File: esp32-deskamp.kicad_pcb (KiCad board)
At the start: 2 copper layers, 35 parts, among them J1 INPUT 00, J10 ADDITIONAL GPIO, J2 INPUT 01, J3 MUTE, J4 SLEEP, J5 PRE OUT, J6 LFE OUT, J7 INPUT SELECT, J8 MOTOR, J9 12V IN, K1 INPUT 00, K2 INPUT 01, K3 AMP MUTE, K4 AMP SLEEP, Q1 2N3904, Q2 2N3904, Q3 2N3904, Q4 2N3904, U1 ESP32 D1 MINI, U2 TSR 1-2433, U3 L9110

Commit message: Break time
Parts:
- moved J10 130.6 mm to (180.0, 84.5), turned to 90 degrees
- moved Q4 113.3 mm to (180.0, 132.5), turned to 90 degrees
- moved Q3 113.0 mm to (180.0, 120.5), turned to 90 degrees
- moved R4 108.4 mm to (180.0, 136.6), turned to -90 degrees
- moved R3 106.9 mm to (180.0, 124.8), turned to 90 degrees
- moved R2 106.2 mm to (180.0, 113.5), turned to -90 degrees
- moved U1 98.2 mm to (157.3, 92.2), turned to 0 degrees
- moved J7 85.5 mm to (192.2, 77.0), turned to 180 degrees
- moved K4 81.6 mm to (188.9, 137.5), turned to 90 degrees
- moved D4 81.2 mm to (184.6, 137.5), turned to 90 degrees
- moved J9 80.1 mm to (135.0, 107.3), turned to 90 degrees
- moved U2 78.0 mm to (136.4, 96.2)
- moved J4 65.8 mm to (134.2, 137.3), turned to 90 degrees
- moved K3 65.1 mm to (189.0, 125.5), turned to 90 degrees
- moved D3 64.4 mm to (184.7, 125.5), turned to 90 degrees
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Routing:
- net +12V: track 8.72 -> 58.4 mm
- net Net-(J2-Pin_1): track 0.00 -> 48.4 mm
- net Net-(J1-Pin_1): track 0.00 -> 31.2 mm
- net Net-(J1-Pin_2): track 0.00 -> 30.7 mm
- net Net-(J2-Pin_2): track 22.2 -> 44.6 mm
- net PRE_LEFT: track 0.00 -> 12.5 mm
- net PRE_RIGHT: track 0.00 -> 12.5 mm
- net Select2: track 0.00 -> 10.2 mm
- net Net-(D3-A): track 0.00 -> 9.46 mm
- net Net-(D4-A): track 0.00 -> 9.13 mm
- net Net-(J6-Pin_2): track 28.7 -> 19.8 mm
- net Select1: track 0.00 -> 8.18 mm
- net Net-(Q2-B): track 0.00 -> 5.96 mm
- net Net-(Q1-B): track 0.00 -> 5.96 mm
- net Select0: track 0.00 -> 5.50 mm
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
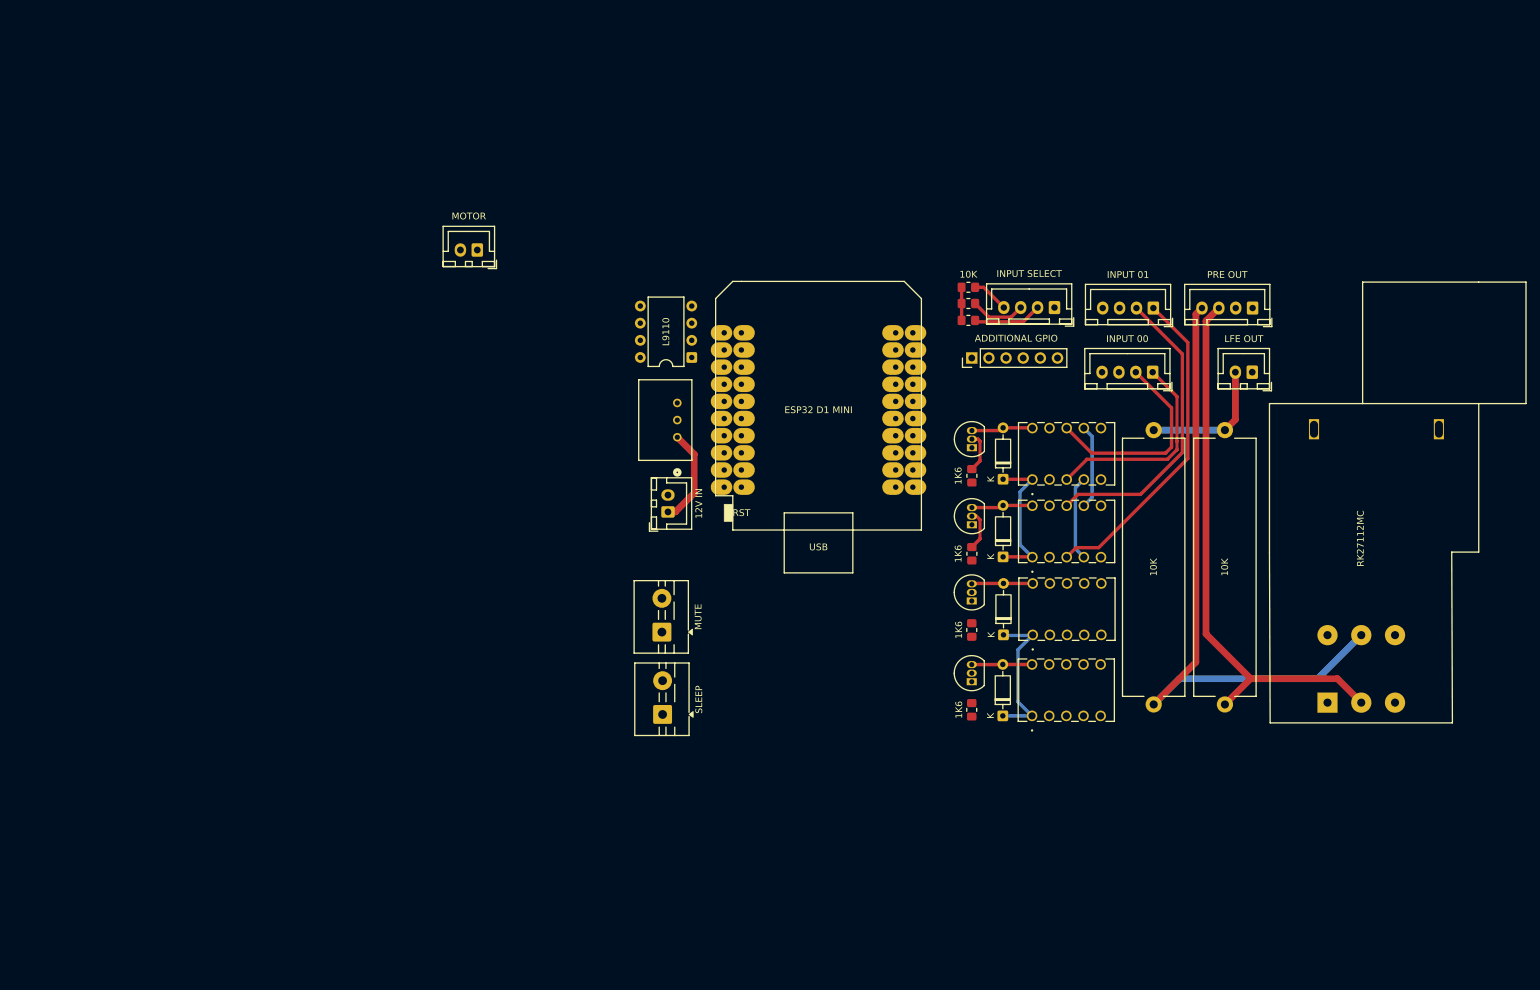
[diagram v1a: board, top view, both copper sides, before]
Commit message: Locked in routing for relays
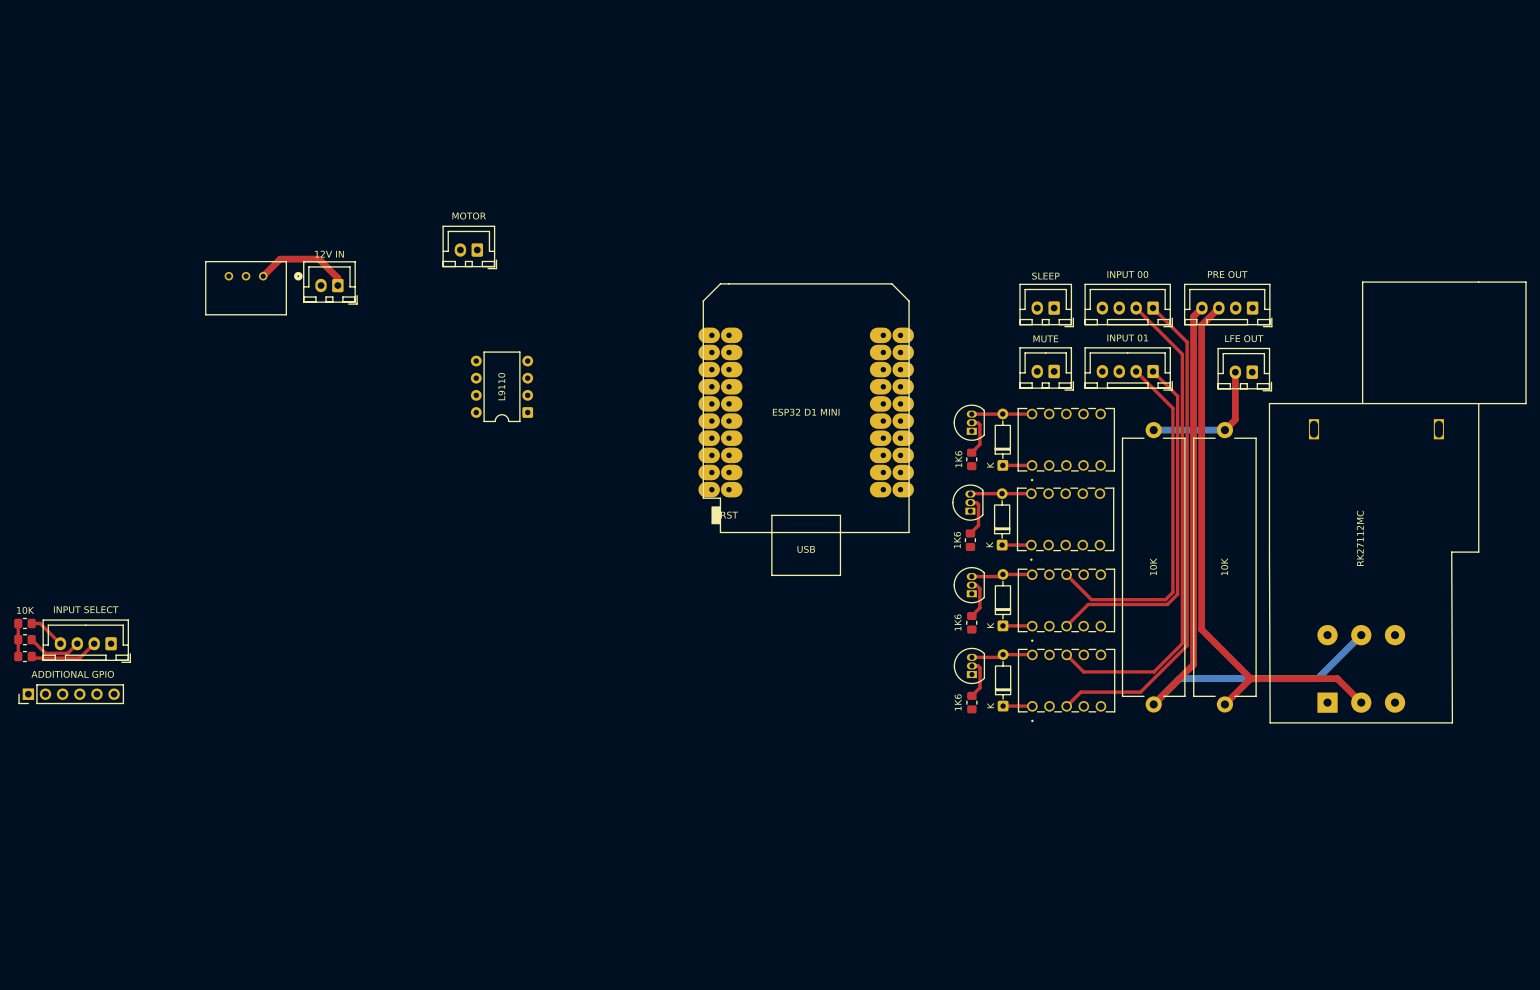
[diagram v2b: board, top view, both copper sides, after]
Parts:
- J3, J4: footprint TerminalBlock:TerminalBlock_MaiXu_MX126-5.0-02P_1x02_P5.00mm -> Connector_JST:JST_XH_B2B-XH-A_1x02_P2.50mm_Vertical
- moved J10 148.4 mm to (40.2, 134.3)
- moved J7 148.4 mm to (52.5, 126.8)
- moved R7 148.4 mm to (39.7, 128.7)
- moved R8 148.4 mm to (39.7, 126.2)
- moved R9 148.4 mm to (39.7, 123.8)
- moved J4 83.6 mm to (192.2, 77.1), turned to 180 degrees
- moved J3 69.8 mm to (192.2, 86.5), turned to 180 degrees
- moved U2 65.8 mm to (75.0, 72.4), turned to 180 degrees
- moved J9 59.3 mm to (86.1, 73.8), turned to 180 degrees
- moved K4 37.1 mm to (188.9, 100.4)
- moved Q4 37.1 mm to (180.0, 95.4)
- moved R4 37.1 mm to (180.0, 99.5)
- moved D4 37.1 mm to (184.6, 100.4)
- moved Q1 33.6 mm to (180.0, 131.4)
- moved D1 33.6 mm to (184.6, 136.1)
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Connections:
- K3 pad 3: Net-(J3-Pin_1) -> Net-(J3-Pin_2)
- K3 pad 4: Net-(J3-Pin_2) -> Net-(J3-Pin_1)
- K4 pad 3: Net-(J4-Pin_1) -> Net-(J4-Pin_2)
- K4 pad 4: Net-(J4-Pin_2) -> Net-(J4-Pin_1)
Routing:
- net Net-(J1-Pin_1): track 31.2 -> 73.7 mm
- net Net-(J1-Pin_2): track 30.7 -> 72.5 mm
- net +12V: track 58.4 -> 31.6 mm
- net PRE_LEFT: track 12.5 -> 0.00 mm
- net PRE_RIGHT: track 12.5 -> 0.00 mm
- net Net-(J2-Pin_2): track 44.6 -> 52.7 mm
- net Net-(Q3-B): track 0.00 -> 6.10 mm
- net Net-(Q4-B): track 0.00 -> 5.96 mm
- net Net-(J2-Pin_1): track 48.4 -> 52.9 mm
- net Net-(J5-Pin_3): track 81.7 -> 82.2 mm

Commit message: Milestone, may tweak layout
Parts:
- moved J10 100.5 mm to (132.5, 94.3), turned to 0 degrees
- moved U2 88.7 mm to (149.5, 120.5)
- moved J9 84.4 mm to (146.8, 132.5)
- moved R9 83.9 mm to (114.9, 86.5), turned to -90 degrees
- moved R8 82.9 mm to (112.5, 86.5), turned to -90 degrees
- moved R7 82.0 mm to (110.0, 86.5), turned to -90 degrees
- moved J7 63.9 mm to (112.0, 103.5), turned to 90 degrees
- moved U3 60.4 mm to (168.5, 119.0), turned to -90 degrees
- moved U1 2.53 mm to (158.0, 92.6)
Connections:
- RV1 pad 1: PRE_LEFT -> PRE_RIGHT
- RV1 pad 4: PRE_RIGHT -> PRE_LEFT
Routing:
- net PRE_LEFT: track 0.00 -> 71.3 mm
- net PRE_RIGHT: track 0.00 -> 52.1 mm
- net Net-(J3-Pin_2): track 0.00 -> 43.0 mm
- net Net-(J4-Pin_2): track 0.00 -> 40.6 mm
- net Net-(J3-Pin_1): track 0.00 -> 39.7 mm
- net Net-(J4-Pin_1): track 0.00 -> 38.2 mm
- net Select2: track 10.2 -> 0.00 mm
- net Select1: track 8.18 -> 0.00 mm
- net Select0: track 5.50 -> 0.00 mm
- net +3V3: track 4.90 -> 0.00 mm
- net Net-(J5-Pin_3): track 82.2 -> 84.5 mm
- net +12V: track 31.6 -> 30.4 mm

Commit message: V3
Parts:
- removed Q1, Q2, Q3, Q4: 2N3904, Package_TO_SOT_THT:TO-92_Inline
- removed R1, R2, R3, R4: 1K6, Resistor_SMD:R_0805_2012Metric_Pad1.20x1.40mm_HandSolder
- added ? (x3): , , F.Cu at (201.2, 38.5)
- added ? (x2): , , F.Cu at (99.8, 38.5)
- added ?: , , F.Cu at (110.0, 96.2)
- added C1: 10uF, Capacitor_THT:DX_5R5VxxxxU_D11.5mm_P5.00mm, F.Cu at (116.5, 60.3)
- added REF**: MountingHole_3.2mm_M3_DIN965_Pad_TopOnly, MountingHole:MountingHole_3.2mm_M3_DIN965_Pad_TopOnly, F.Cu at (226.8, 96.2)
- added REF**: MountingHole_3.2mm_M3_DIN965_Pad_TopOnly, MountingHole:MountingHole_3.2mm_M3_DIN965_Pad_TopOnly, F.Cu at (99.8, 38.5)
- added REF**: MountingHole_3.2mm_M3_DIN965_Pad_TopOnly, MountingHole:MountingHole_3.2mm_M3_DIN965_Pad_TopOnly, F.Cu at (201.2, 38.5)
- added REF**: MountingHole_3.2mm_M3_DIN965_Pad_TopOnly, MountingHole:MountingHole_3.2mm_M3_DIN965_Pad_TopOnly, F.Cu at (110.0, 96.2)
- added U4: ULN2003A, Package_SO:SSOP-16_4.4x5.2mm_P0.65mm, F.Cu at (127.0, 63.0)
- moved D3 112.0 mm to (88.3, 54.9)
- moved K3 112.0 mm to (92.6, 54.9)
- moved J9 107.5 mm to (92.5, 39.7)
- moved K1 96.9 mm to (135.7, 55.2)
- moved D1 96.7 mm to (131.6, 55.2)
- moved J3 94.3 mm to (110.5, 39.5)
- moved D4 87.5 mm to (109.9, 54.9)
- moved K4 87.5 mm to (114.2, 54.9)
- moved J4 79.2 mm to (122.5, 39.5)
- moved K2 75.9 mm to (157.4, 55.2)
- moved D2 75.8 mm to (153.2, 55.2)
- moved J1 73.2 mm to (144.2, 39.2)
- moved U3 68.4 mm to (112.5, 79.8), turned to 0 degrees
- moved J2 62.3 mm to (166.2, 39.2)
- moved U2 59.1 mm to (112.4, 74.5), turned to 0 degrees
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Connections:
- net Net-(D1-A) renamed Relay0
- net Net-(D2-A) renamed Relay1
- net Net-(D3-A) renamed Relay2
- net Net-(D4-A) renamed Relay3
- J5 pad 1: GNDA -> Net-(J5-Pin_1)
- J5 pad 2: GNDA -> Net-(J5-Pin_2)
- J5 pad 3: Net-(J5-Pin_3) -> GNDA
- J5 pad 4: Net-(J5-Pin_4) -> GNDA
- J6 pad 1: GNDA -> Net-(J6-Pin_1)
- J6 pad 2: Net-(J6-Pin_2) -> GNDA
- R5 pad 1: Net-(J6-Pin_2) -> Net-(J6-Pin_1)
- R5 pad 2: Net-(J5-Pin_3) -> Net-(J5-Pin_2)
- R6 pad 1: Net-(J6-Pin_2) -> Net-(J6-Pin_1)
- R6 pad 2: Net-(J5-Pin_4) -> Net-(J5-Pin_1)
- RV1 pad 2: Net-(J5-Pin_3) -> Net-(J5-Pin_2)
- RV1 pad 5: Net-(J5-Pin_4) -> Net-(J5-Pin_1)
- U3 pad 1: Net-(J8-Pin_1) -> Net-(J8-Pin_2)
- U3 pad 4: Net-(J8-Pin_2) -> Net-(J8-Pin_1)
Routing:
- net +12V: track 30.4 -> 147.3 mm
- net Net-(J5-Pin_4): track 96.7 -> 0.00 mm
- net Net-(J5-Pin_2): track 0.00 -> 95.9 mm
- net Net-(J5-Pin_1): track 0.00 -> 85.9 mm
- net Net-(J5-Pin_3): track 84.5 -> 0.00 mm
- net Net-(J1-Pin_2): track 72.5 -> 8.80 mm
- net Net-(J1-Pin_1): track 73.7 -> 20.6 mm
- net +3V3: track 0.00 -> 45.7 mm
- net Net-(J2-Pin_2): track 52.7 -> 9.22 mm
- net Relay2: track 9.46 -> 52.6 mm, vias 0 -> 1
- net PRE_RIGHT: track 52.1 -> 93.0 mm
- net Net-(J2-Pin_1): track 52.9 -> 20.9 mm
- net Net-(J6-Pin_1): track 0.00 -> 31.6 mm
- net Relay1: track 9.18 -> 36.4 mm, vias 0 -> 1
- net PRE_LEFT: track 71.3 -> 96.2 mm
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- added copper zone on B.Cu, net GNDA
- added copper zone on B.Cu, net GNDS
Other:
- board outline added: 145.2 x 66.5 mm
- board text added: "+"
- board text added: "-"
- board text added: "GNDA"
- board text added: "L"
- board text added: "R"
- board text added: "–"

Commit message: Moar routing
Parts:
- moved R7 27.8 mm to (97.0, 84.5)
- moved R8 27.8 mm to (101.5, 84.5)
- moved R9 27.8 mm to (99.2, 84.5)
- moved J10 5.37 mm to (160.0, 97.0), turned to -90 degrees
- moved U2 2.25 mm to (114.7, 74.5)
- moved J7 0.75 mm to (100.2, 64.5)
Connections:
- U3 pad 6: PWM0 -> PWM1
- U3 pad 7: PWM1 -> PWM0
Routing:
- net PWM1: track 0.00 -> 34.9 mm
- net PWM0: track 0.00 -> 32.9 mm
- net Net-(J8-Pin_2): track 0.00 -> 20.1 mm
- net Net-(J8-Pin_1): track 0.00 -> 12.0 mm
- net PRE_RIGHT: track 93.0 -> 102.1 mm
- net +3V3: track 45.7 -> 41.4 mm
- net Input1: track 0.00 -> 2.90 mm, vias 0 -> 1
- net Sleep: track 0.00 -> 1.27 mm
- net Mute: track 0.00 -> 1.27 mm
- net Net-(J5-Pin_2): track 95.9 -> 94.9 mm
- net Input0: track 0.00 -> 1.07 mm
- net +12V: track 147.3 -> 148.3 mm

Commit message: Enough for tonight, routed relay control board
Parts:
- moved R9 7.67 mm to (96.8, 77.2), turned to 180 degrees
- moved R8 6.90 mm to (96.8, 79.5), turned to 180 degrees
- moved R7 2.76 mm to (96.8, 81.8), turned to 180 degrees
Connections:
- U1 pad 29: Mute -> Sleep
- U1 pad 31: Sleep -> Mute
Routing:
- net Input0: track 1.07 -> 37.4 mm, vias 0 -> 1
- net Sleep: track 1.27 -> 36.6 mm, vias 0 -> 1
- net Input1: track 2.90 -> 38.0 mm
- net Mute: track 1.27 -> 36.2 mm, vias 0 -> 1
